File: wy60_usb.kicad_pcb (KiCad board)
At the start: 2 copper layers, 409.1 x 170.9 mm, 223 parts, among them J1 AVR-ISP-6, U1 ATmega32A-PU

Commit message: add gerbers and readme
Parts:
- renumbered D110 to D100, D111 to D101, D112 to D102, D113 to D103, D12 to D11, D13 to D12, D14 to D13, D15 to D14, D16 to D15, D17 to D16, D18 to D17, D19 to D18, D20 to D19, D21 to D20, D22 to D21, D23 to D22, D24 to D23, D25 to D24, D26 to D25, D27 to D26, D28 to D27, D29 to D28, D30 to D29, D31 to D30, D32 to D31, D33 to D32, D34 to D33, D35 to D34, D36 to D35, D37 to D36, D38 to D37, D39 to D38, D40 to D39, D41 to D40, D42 to D41, D43 to D42, D44 to D43, D45 to D44, D46 to D45, D47 to D46, D48 to D47, D49 to D48, D50 to D49, D51 to D50, D52 to D51, D53 to D52, D54 to D53, D55 to D54, D56 to D55, D57 to D56, D58 to D57, D59 to D58, D60 to D59, D61 to D60, D62 to D61, D63 to D62, D64 to D63, D65 to D64, D66 to D65, D67 to D66, D68 to D67, D69 to D68, D70 to D69, D71 to D70, D72 to D71, D74 to D72, D75 to D73, D76 to D74, D77 to D75, D78 to D76, D79 to D77, D80 to D78, D81 to D79, D82 to D80, D83 to D81, D84 to D82, D85 to D83, D86 to D84, D87 to D85, D88 to D86, D89 to D87, D90 to D88, D91 to D89, D92 to D90, D93 to D91, D94 to D92, D95 to D93, D96 to D94, D97 to D95, D98 to D96, D104 to D97, D108 to D98, D109 to D99, MX11 to MX10, MX110 to MX100, MX111 to MX101, MX12 to MX11, MX13 to MX12, MX14 to MX13, MX15 to MX14, MX16 to MX15, MX17 to MX16, MX18 to MX17, MX19 to MX18, MX20 to MX19, MX21 to MX20, MX22 to MX21, MX23 to MX22, MX24 to MX23, MX25 to MX24, MX26 to MX25, MX27 to MX26, MX28 to MX27, MX29 to MX28, MX30 to MX29, MX31 to MX30, MX32 to MX31, MX33 to MX32, MX34 to MX33, MX35 to MX34, MX36 to MX35, MX37 to MX36, MX38 to MX37, MX39 to MX38, MX40 to MX39, MX41 to MX40, MX42 to MX41, MX43 to MX42, MX44 to MX43, MX45 to MX44, MX46 to MX45, MX47 to MX46, MX48 to MX47, MX49 to MX48, MX50 to MX49, MX51 to MX50, MX52 to MX51, MX53 to MX52, MX54 to MX53, MX55 to MX54, MX56 to MX55, MX57 to MX56, MX58 to MX57, MX59 to MX58, MX60 to MX59, MX61 to MX60, MX62 to MX61, MX63 to MX62, MX64 to MX63, MX65 to MX64, MX66 to MX65, MX67 to MX66, MX68 to MX67, MX69 to MX68, MX70 to MX69, MX72 to MX70, MX73 to MX71, MX74 to MX72, MX75 to MX73, MX76 to MX74, MX77 to MX75, MX78 to MX76, MX79 to MX77, MX80 to MX78, MX81 to MX79, MX82 to MX80, MX83 to MX81, MX84 to MX82, MX85 to MX83, MX86 to MX84, MX87 to MX85, MX88 to MX86, MX89 to MX87, MX90 to MX88, MX91 to MX89, MX10 to MX9, MX92 to MX90, MX93 to MX91, MX94 to MX92, MX95 to MX93, MX96 to MX94, MX102 to MX95, MX106 to MX96, MX107 to MX97, MX108 to MX98, MX109 to MX99
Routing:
- net Net-(D1-Pad1): track 68.3 -> 75.4 mm
- net col11: track 125.5 -> 131.6 mm
- net D-: track 150.5 -> 156.6 mm
- net col13: track 154.6 -> 159.2 mm
- net col1: track 343.7 -> 347.9 mm
- net col16: track 181.7 -> 185.7 mm
- net col17: track 211.6 -> 215.6 mm
- net col18: track 210.0 -> 214.0 mm
- net col2: track 309.8 -> 313.7 mm
- net col19: track 247.8 -> 251.6 mm
- net col7: track 246.3 -> 249.6 mm
- net col6: track 247.0 -> 250.3 mm
- net col8: track 205.9 -> 209.2 mm
- net col10: track 173.0 -> 176.3 mm
- net col4: track 283.6 -> 286.7 mm
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
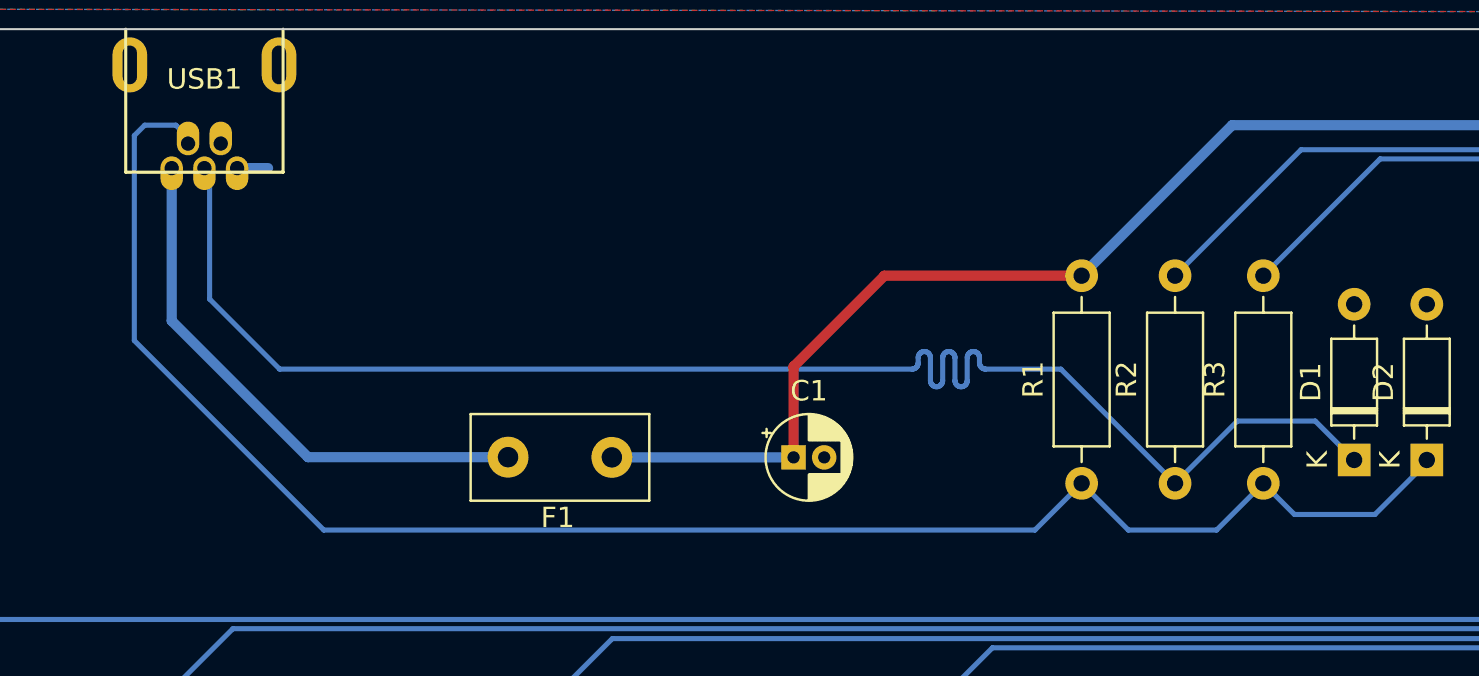
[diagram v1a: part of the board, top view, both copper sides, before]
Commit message: fixed USB orientation
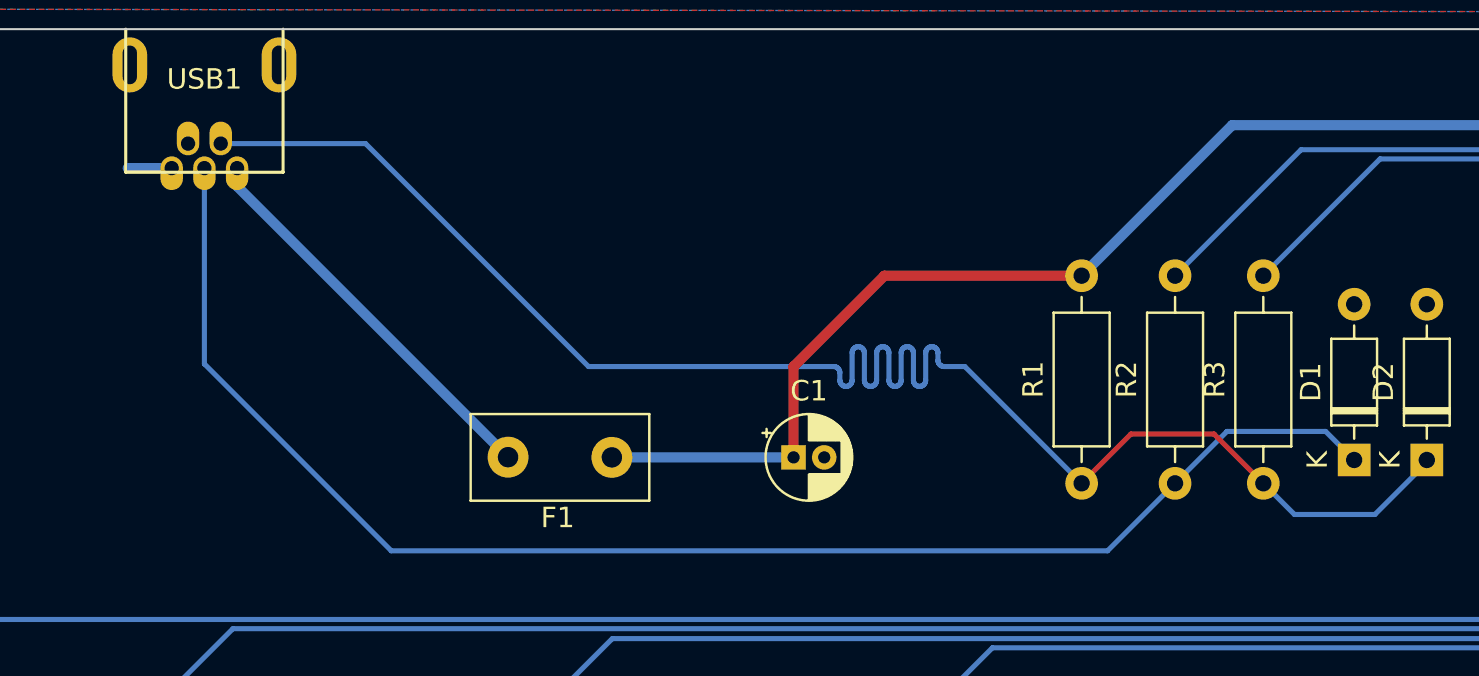
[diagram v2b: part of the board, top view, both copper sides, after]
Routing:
- net VCC: track 26.7 -> 19.6 mm
- net Net-(D1-Pad1): track 75.4 -> 72.6 mm
- net Net-(D2-Pad1): track 85.2 -> 82.9 mm
- net GND: track 1.70 -> 2.33 mm

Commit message: rev2
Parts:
- moved C3 8.89 mm to (256.9, 69.1)
- moved G*** 7.15 mm to (125.0, 63.5)
- moved G*** 7.15 mm to (147.7, 63.4)
- moved R4 4.64 mm to (326.9, 70.1)
- moved Boot1 4.51 mm to (325.4, 60.3)
- moved Reset1 4.51 mm to (312.4, 60.3)
- moved C1 3.82 mm to (72.5, 67.3)
- moved D1 3.82 mm to (99.9, 67.4)
- moved D2 3.82 mm to (103.5, 67.4)
- moved F1 3.82 mm to (63.6, 67.3)
- moved R1 3.82 mm to (86.6, 68.6)
- moved R2 3.82 mm to (91.2, 68.6)
- moved R3 3.82 mm to (95.5, 68.6)
- moved C2 2.92 mm to (259.3, 53.7)
- moved C5 2.80 mm to (286.8, 56.8)
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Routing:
- net +5V: track 359.7 -> 347.4 mm
- net col15: track 139.2 -> 146.7 mm
- net row3: track 475.3 -> 481.5 mm
- net row4: track 489.1 -> 495.2 mm
- net row1: track 450.1 -> 455.9 mm
- net row5: track 532.5 -> 537.3 mm
- net row2: track 460.0 -> 464.6 mm
- net col2: track 313.7 -> 309.7 mm
- net col1: track 347.9 -> 344.2 mm
- net col4: track 286.7 -> 283.4 mm
- net col3: track 303.0 -> 299.8 mm
- net col14: track 134.4 -> 137.6 mm
- net col11: track 131.6 -> 134.8 mm
- net col7: track 249.6 -> 246.5 mm
- net col6: track 250.3 -> 247.5 mm
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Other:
- board size 409.1 x 170.9 mm -> 407.9 x 170.4 mm
- board text added: "WY-60 USB PCB rev. 2 github.com/kb-elmo/wy60_usb elmo.space"
- board text removed: "WY-60 USB PCB rev. 1 github.com/kb-elmo/wy60_usb elmo.space"

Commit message: fixed spacing
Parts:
- moved MX71 0.23 mm to (337.5, 162.3)
- moved MX72 0.23 mm to (356.5, 162.3)
- moved MX34 0.23 mm to (337.5, 124.2)
- moved MX35 0.23 mm to (356.5, 124.2)
- moved D36 0.23 mm to (327.9, 129.7)
- moved D37 0.23 mm to (347.0, 129.7)
- moved D55 0.23 mm to (327.9, 148.5)
- moved D56 0.23 mm to (347.0, 148.5)
- moved D73 0.23 mm to (327.9, 167.6)
- moved D74 0.23 mm to (347.0, 167.6)
- moved D92 0.23 mm to (327.9, 186.6)
- moved D93 0.23 mm to (347.0, 186.6)
- moved MX53 0.23 mm to (337.5, 143.2)
- moved MX54 0.23 mm to (356.5, 143.2)
- moved MX90 0.23 mm to (337.5, 181.3)
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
